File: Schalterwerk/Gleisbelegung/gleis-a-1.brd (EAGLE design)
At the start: 100.3 x 80 mm, 55 parts, among them J1 PHNX_4P_508CONN_1017493, J2 PHNX_4P_508CONN_1017493, J3 PHNX_2P_508CONN_1017491, J4 PHNX_4P_350CONN_1984989_PXC, J5 PHNX_4P_350CONN_1984989_PXC, Q1 P-MOSFET, Q2 P-MOSFET, Q3 P-MOSFET, Q4 P-MOSFET, X1 RJ45-JACK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

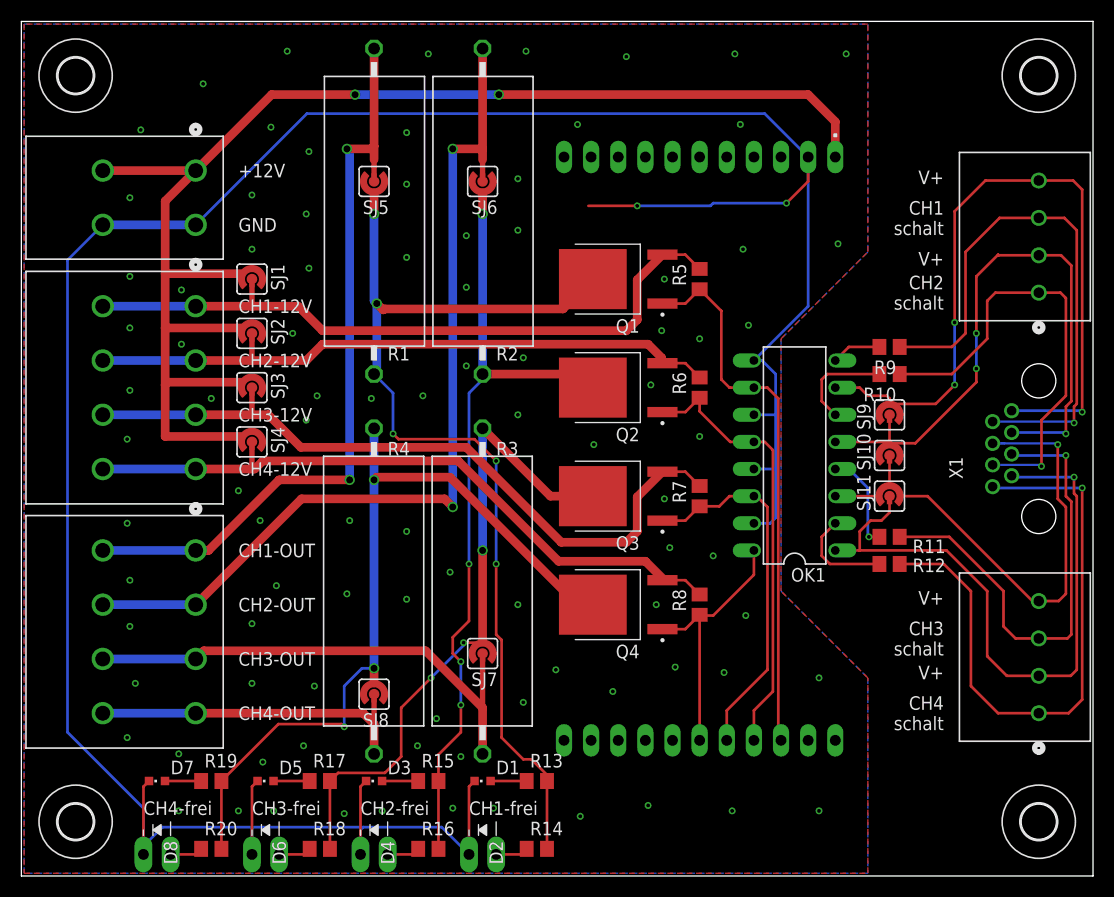
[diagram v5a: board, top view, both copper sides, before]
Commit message: Finalizes first version of the gleisbelegung board. Adds gerbers.
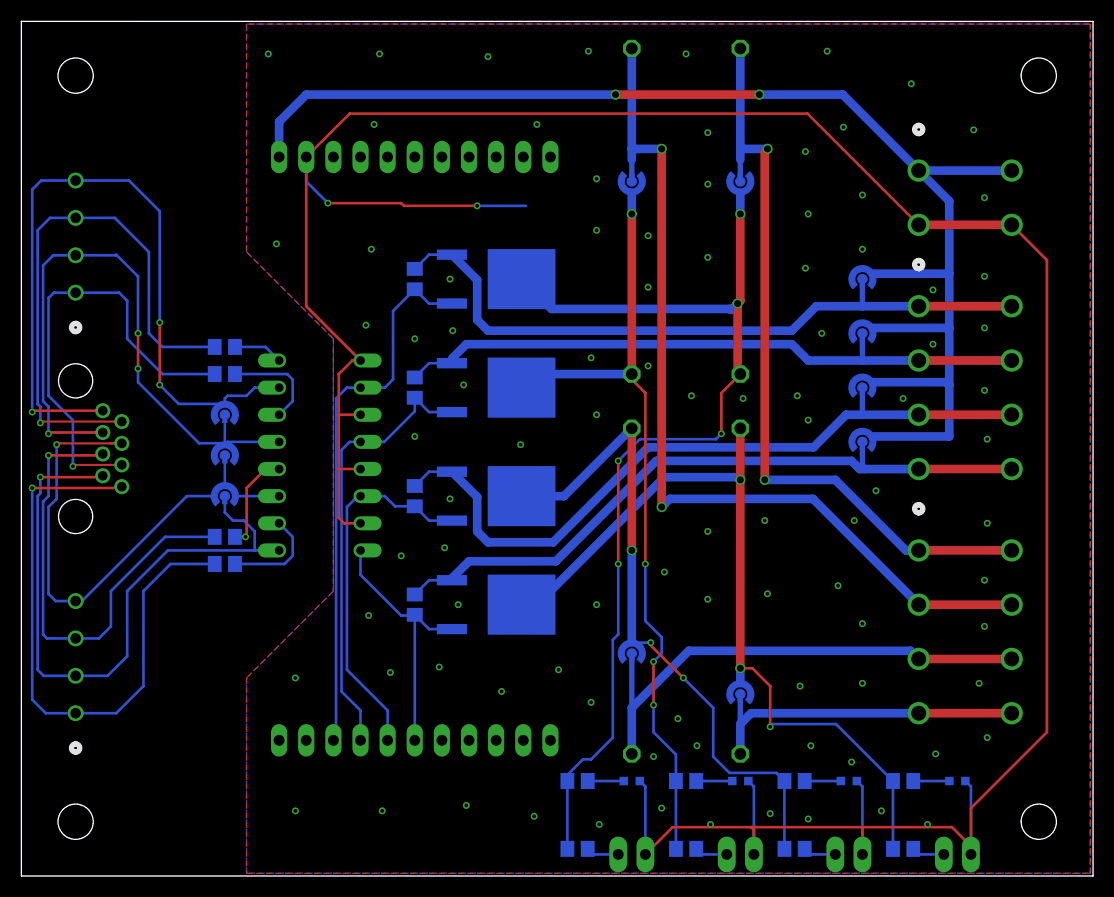
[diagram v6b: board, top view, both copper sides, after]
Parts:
- moved H1 90.2 mm to (5.08, 74.9), flipped to the bottom
- moved H2 90.2 mm to (5.08, 5.08), flipped to the bottom
- moved H3 90.2 mm to (95.2, 5.08), flipped to the bottom
- moved H4 90.2 mm to (95.2, 74.9), flipped to the bottom
- moved J4 90.2 mm to (5.08, 54.6), flipped to the bottom
- moved J5 90.2 mm to (5.08, 15.2), flipped to the bottom
- moved X1 90.2 mm to (5.08, 40.0), flipped to the bottom
- moved J1 85.1 mm to (92.7, 38.1), flipped to the bottom
- moved J2 85.1 mm to (92.7, 15.2), flipped to the bottom
- moved J3 85.1 mm to (92.7, 61.0), flipped to the bottom
- moved D7 74.9 mm to (87.6, 8.89), flipped to the bottom
- moved D8 74.9 mm to (87.6, 2.02), flipped to the bottom
- moved R19 64.8 mm to (82.5, 8.89), flipped to the bottom
- moved R20 64.8 mm to (82.5, 2.54), flipped to the bottom
- moved R10 62.2 mm to (19.1, 47.0), flipped to the bottom
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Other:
- board text added: "(c) Balazs Racz 20230526"
- board text added: "CH1"
- board text added: "CH2"
- board text added: "CH3"
- board text added: "CH4"
- board text added: "Farben nach 568B"
- board text added: "Gleisfreimeldung"
- board text added: "IO board nach oben"
- board text added: "Licht=frei"
- board text added: "Schaltausgänge vom Digitaldecoder anbinden."
- board text added: "bl/w|"
- board text added: "bl|"
- board text added: "br/w|"
- board text added: "br|"
- board text added: "gn/w|"
- board text added: "gn|"
- board text added: "ora/w|"
- board text added: "ora|"
- board text removed: "CH1-frei"
- board text removed: "CH2-frei"
- board text removed: "CH3-frei"
- board text removed: "CH4-frei"
